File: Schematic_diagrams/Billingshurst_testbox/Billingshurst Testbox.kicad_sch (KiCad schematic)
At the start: 33 parts, among them J10 Conn_01x15_Socket, J3 D Sub Conn_15_Pin Female, J4 Conn_01x07_Socket, J5 Conn_7_Pin, K1 UP relay module ch.8, SW4 SW_Push

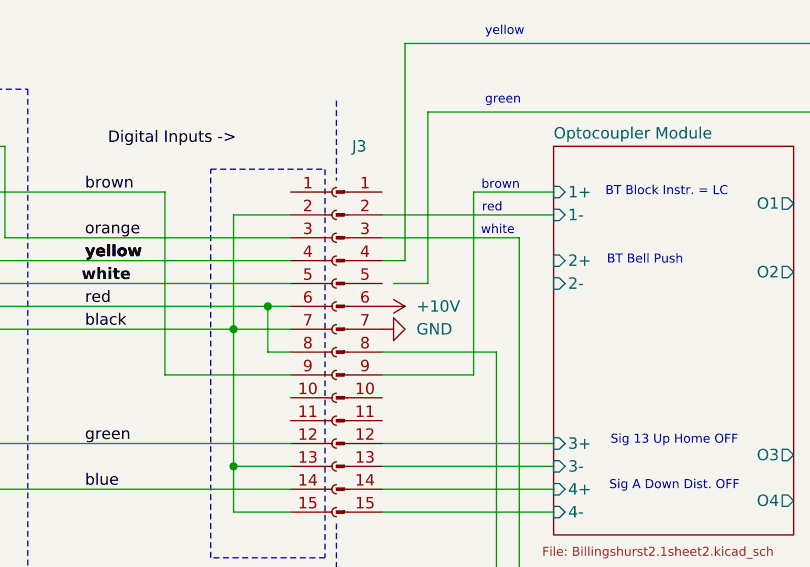
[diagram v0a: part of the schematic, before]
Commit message: general changes
update to relay module input name
new schematic: internal signal box model signal control
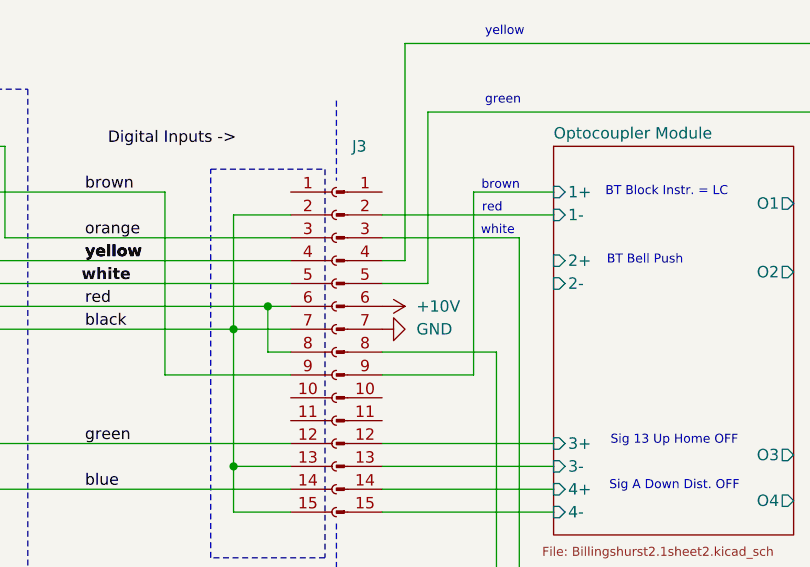
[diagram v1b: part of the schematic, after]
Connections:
- net 0V: now also J3.5 (Pin_5)
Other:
- title: Billingshurst Testbox -> Billingshurst Testbox - Connections to Main Controller
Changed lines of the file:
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@@
 	(paper "A4")
 	(title_block
-		(title "Billingshurst Testbox")
+		(title "Billingshurst Testbox - Connections to Main Controller")
 		(date "19/12/2025")
 		(rev "A")
@@
 	(wire
 		(pts
+			(xy 172.72 49.53) (xy 177.8 49.53)
+		)
+		(stroke
+			(width 0)
+			(type default)
+		)
+	)
+	(wire
+		(pts
 			(xy 162.56 49.53) (xy 104.14 49.53)
 		)
@@
 		)
 		(stroke
-			(width 0)
-			(type default)
-		)
-	)
-	(wire
-		(pts
-			(xy 173.99 49.53) (xy 177.8 49.53)
-		)
-		(stroke
